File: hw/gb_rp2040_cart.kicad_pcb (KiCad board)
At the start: 2 copper layers, 51.4 x 60.5 mm, 66 parts, among them J1 GameBoy_Cartridge, J2 USB_C_Receptacle_USB2.0, Q1 SI2301CDS-T1-GE3, Q2 N-Channel, SW1 SW_SPST, U1 SN74LVC8T245PW, U10 MB85RC256VPNF-G-JNERE1, U2 SN74LVC8T245PW, U3 TXU0104, U4 SN74LVC8T245PW, U5 W25Q128JVSIQ, U6 RP2040, U7 AMS1117-3.3, U8 RV-3129-C3, U9 PCA9536D, Y1 Crystal_GND24

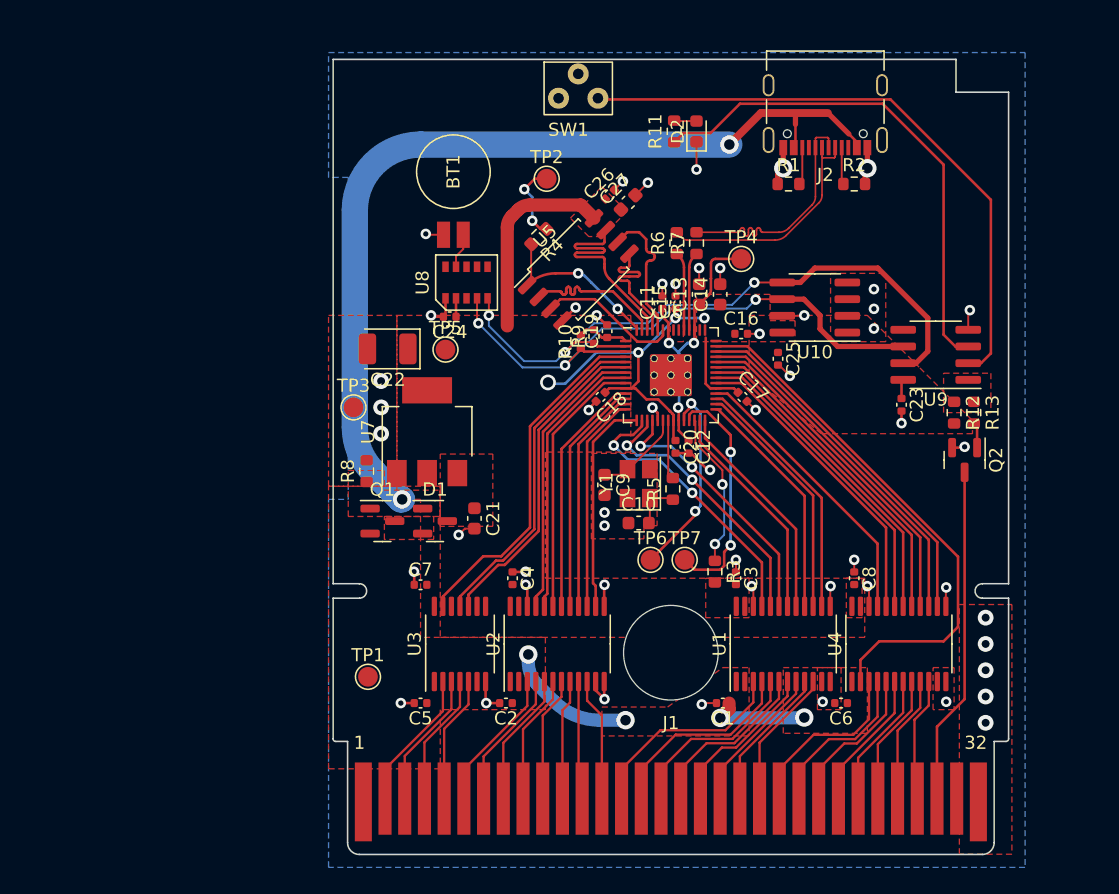
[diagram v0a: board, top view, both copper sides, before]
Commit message: hw: replace RTC
Signed-off-by: Mahyar Koshkouei <mk@deltabeard.com>
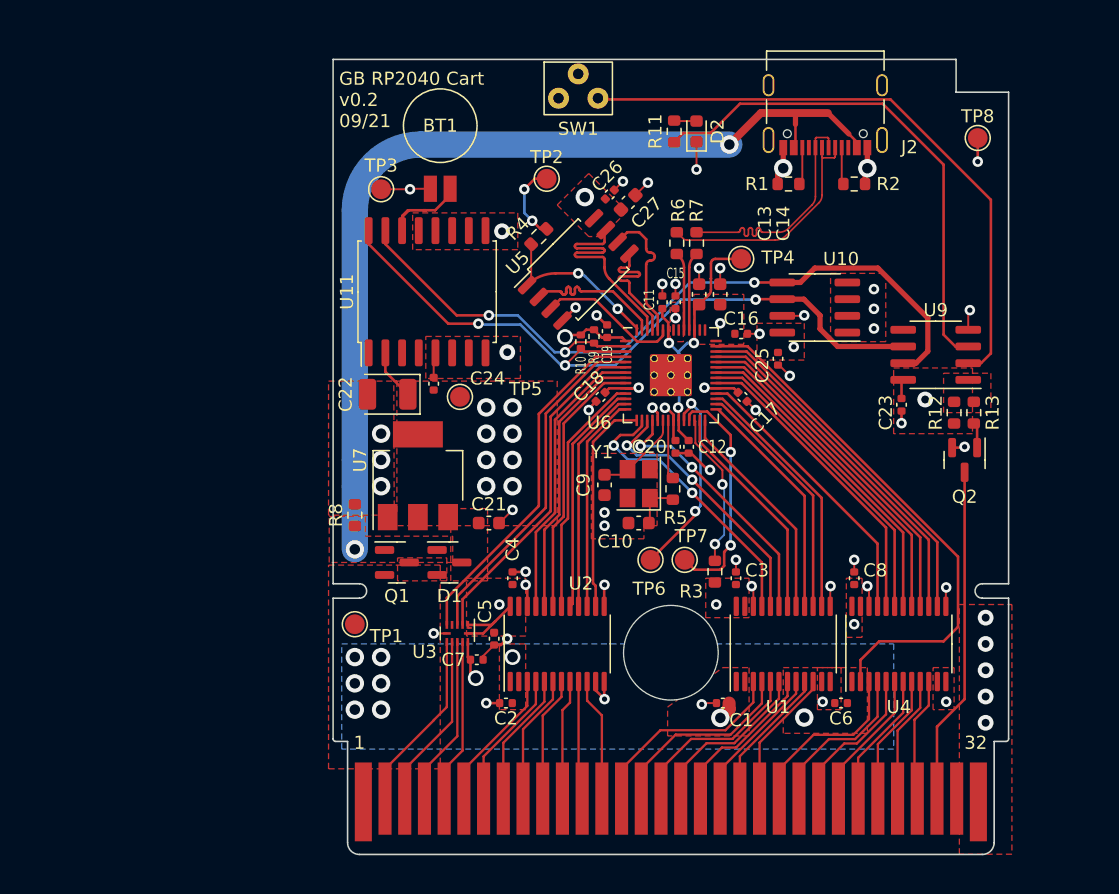
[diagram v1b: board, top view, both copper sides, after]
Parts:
- removed U8: RV-3129-C3, Project_Specific:SOIC-10_RV-3129-C3
- added TP8: GND, TestPoint:TestPoint_Pad_D1.5mm, F.Cu at (107.4, 43.5)
- added U11: DS3231M, Package_SO:SOIC-16W_7.5x10.3mm_P1.27mm, F.Cu at (65.5, 55.2)
- U3: value TXU0104 -> TXB0104RUT; footprint Package_SO:TSSOP-14_4.4x5mm_P0.65mm -> Package_DFN_QFN:Texas_R_PUQFN-N12
- moved TP3 16.7 mm to (62.0, 47.4)
- moved C5 7.44 mm to (70.6, 81.6), turned to -90 degrees
- moved C7 7.13 mm to (69.3, 83.2), turned to 180 degrees
- moved C24 5.24 mm to (66.0, 62.2), turned to 90 degrees
- moved TP1 4.12 mm to (60.0, 80.5)
- moved TP5 3.76 mm to (68.0, 63.2)
- moved BT1 3.64 mm to (66.5, 47.4)
- moved R8 3.47 mm to (60.0, 72.2)
- moved C22 3.45 mm to (62.5, 63.0)
- moved U7 3.42 mm to (64.8, 69.2)
- moved D1 3.34 mm to (67.2, 75.8)
- moved Q1 3.34 mm to (63.2, 75.8)
- moved C21 1.15 mm to (70.2, 72.8), turned to 0 degrees
- moved U3 0.82 mm to (67.8, 81.2), turned to -90 degrees
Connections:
- C5 pad 1: GB_5V -> +3V3
- C7 pad 2: +3V3 -> GB_5V
- U3 pad 1: GB_5V -> +3V3
- U3 pad 10: ~{CS}_3V3 -> ~{CS}
- U3 pad 11: ~{RD}_3V3 -> GB_5V
- U3 pad 12: ~{WR}_3V3 -> +3V3
- U3 pad 2: PHI -> ~{CS}_3V3
- U3 pad 3: ~{WR} -> ~{RD}_3V3
- U3 pad 4: ~{RD} -> ~{WR}_3V3
- U3 pad 5: ~{CS} -> PHI_3V3
- U3 pad 6: (no net) -> GND
- U3 pad 7: GND -> PHI
- U3 pad 8: +3V3 -> ~{WR}
- U3 pad 9: (no net) -> ~{RD}
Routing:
- net +3V3: track 53.9 -> 26.2 mm, vias 4 -> 20
- net GB_5V: track 17.9 -> 4.40 mm, vias 4 -> 10
- net I^{2}C_{SCL}: track 45.1 -> 54.9 mm
- net I^{2}C_{SDA}: track 50.7 -> 59.7 mm
- net Net-(BT1-Pad1): track 2.66 -> 8.99 mm
- net PHI: track 8.48 -> 13.9 mm
- net GND: track 56.2 -> 60.2 mm, vias 53 -> 55
- net ~{WR}: track 10.4 -> 13.4 mm
- net ~{RD}: track 10.0 -> 13.0 mm
- net ~{CS}: track 9.67 -> 12.5 mm
- net VBUS: track 73.7 -> 76.2 mm
- net ~{CS}_3V3: track 24.5 -> 25.9 mm
- net ~{RD}_3V3: track 25.3 -> 26.6 mm
- net PHI_3V3: track 26.7 -> 27.4 mm
- added copper zone on In2.Cu, net +3V3
- added copper zone on B.Cu, net GB_5V
- added copper zone on In1.Cu, net GND
- removed copper zone on B.Cu, net GND
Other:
- copper layers 2 -> 4
- board text added: "Flash cart compatible with DMG, MGB, CGB. Unlicensed product. Using RP2040, with 16MiB NOR, 32KiB FRAM, RTC, USB-C. Design: UK, Assembly: PRC Copyright (c) 2021 Mahyar Koshkouei; Not for resale."
- board text added: "GB RP2040 Cart v0.2 09/21"
- board text added: "JLCJLCJLCJLC"
- board text added: "Order"

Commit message: hw: complete routing
Use components available on LCSC.

Signed-off-by: Mahyar Koshkouei <mk@deltabeard.com>
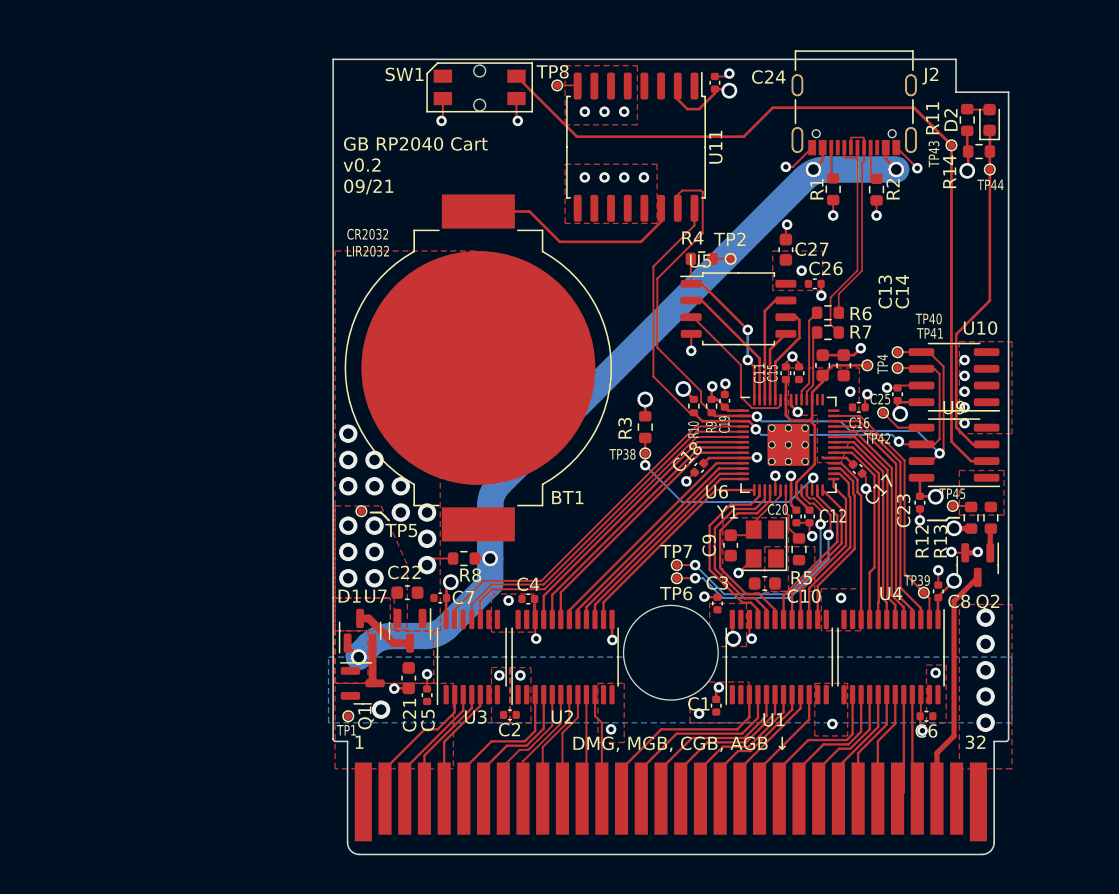
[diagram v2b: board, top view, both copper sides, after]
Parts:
- removed TP3: TestPoint, TestPoint:TestPoint_Pad_D1.5mm
- added R14: 100k, Resistor_SMD:R_0603_1608Metric, F.Cu at (107.5, 44.5)
- added TP38: TestPoint_Small, Project_Specific:TestPoint_Pad_D0.5mm, F.Cu at (82.1, 67.5)
- added TP39: TestPoint_Small, Project_Specific:TestPoint_Pad_D0.5mm, F.Cu at (103.3, 78.1)
- added TP40: TestPoint_Small, Project_Specific:TestPoint_Pad_D0.5mm, F.Cu at (101.3, 59.8)
- added TP41: TestPoint_Small, Project_Specific:TestPoint_Pad_D0.5mm, F.Cu at (101.3, 61.0)
- added TP42: TestPoint_Small, Project_Specific:TestPoint_Pad_D0.5mm, F.Cu at (100.2, 64.4)
- added TP43: TestPoint_Small, Project_Specific:TestPoint_Pad_D0.5mm, F.Cu at (105.4, 44.1)
- added TP44: TestPoint_Small, Project_Specific:TestPoint_Pad_D0.5mm, F.Cu at (108.3, 45.9)
- added TP45: TestPoint_Small, Project_Specific:TestPoint_Pad_D0.5mm, F.Cu at (105.5, 71.5)
- BT1: footprint Project_Specific:BatteryHolder_Seiko_MS621FE -> Battery:BatteryHolder_MPD_BC2003_1x2032
- C13, C14, C21, C27: value 2.2u -> 1u
- C22: value 100u -> 1u; footprint Capacitor_Tantalum_SMD:CP_EIA-3528-15_AVX-H -> Capacitor_SMD:C_0603_1608Metric
- SW1: value SW_SPST -> SW_DPST; footprint Project_Specific:Push_Button-Horizontal-TC-1109DE-C-J -> Project_Specific:K2-1114SA-A4SW-06
- TP1, TP2, TP4, TP5, TP6, TP7, TP8: footprint TestPoint:TestPoint_Pad_D1.5mm -> TestPoint:TestPoint_Pad_D1.0mm
- U3: value TXB0104RUT -> TXU0104; footprint Package_DFN_QFN:Texas_R_PUQFN-N12 -> Package_SO:TSSOP-14_4.4x5mm_P0.65mm
- U7: value AMS1117-3.3 -> XC6206P332MR; footprint Package_TO_SOT_SMD:SOT-223-3_TabPin2 -> Package_TO_SOT_SMD:SOT-23
- moved TP8 32.2 mm to (75.4, 39.5)
- moved C24 31.3 mm to (87.4, 39.3)
- moved D2 22.3 mm to (108.3, 42.1)
- moved R11 22.3 mm to (106.6, 42.1)
- moved U11 19.3 mm to (81.4, 44.2), turned to -90 degrees
- moved C26 17.0 mm to (95.0, 54.6), turned to 0 degrees
- moved TP2 15.3 mm to (88.6, 52.7)
- moved C22 15.2 mm to (64.0, 78.1), turned to 0 degrees
- moved BT1 13.9 mm to (69.4, 61.0)
- moved C21 13.3 mm to (64.1, 84.6), turned to -90 degrees
- moved R6 12.7 mm to (96.0, 56.8), turned to 0 degrees
- moved U5 12.6 mm to (89.2, 56.5), turned to 0 degrees
- moved TP4 12.6 mm to (99.0, 60.8)
- moved C27 12.5 mm to (92.8, 52.0), turned to 90 degrees
- moved R4 12.5 mm to (86.4, 52.7), turned to 180 degrees
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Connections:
- net GB_RESET renamed /Peripherals/GB_RESET
- C5 pad 1: +3V3 -> GB_5V
- C7 pad 2: GB_5V -> +3V3
- D2 pad 1: GND -> /Peripherals/STAT_LED
- R11 pad 1: Net-(R11-Pad1) -> +3V3
- SW1 pad 1: Net-(SW1-Pad1) -> /Peripherals/SWITCH
- SW1 pad 3: (no net) -> /Peripherals/SWITCH
- U3 pad 1: +3V3 -> GB_5V
- U3 pad 10: ~{CS} -> ~{CS}_3V3
- U3 pad 11: GB_5V -> ~{RD}_3V3
- U3 pad 12: +3V3 -> ~{WR}_3V3
- U3 pad 2: ~{CS}_3V3 -> PHI
- U3 pad 3: ~{RD}_3V3 -> ~{WR}
- U3 pad 4: ~{WR}_3V3 -> ~{RD}
- U3 pad 5: PHI_3V3 -> ~{CS}
- U3 pad 6: GND -> (no net)
- U3 pad 7: PHI -> GND
- U3 pad 8: ~{WR} -> +3V3
- U3 pad 9: ~{RD} -> (no net)
- U4 pad 1: GB_5V -> +3V3
- U4 pad 10: /D7 -> 3V3_D0
- U4 pad 14: 3V3_D7 -> /D0
- U4 pad 15: 3V3_D6 -> /D1
- U4 pad 16: 3V3_D5 -> /D2
- U4 pad 17: 3V3_D4 -> /D3
- U4 pad 18: 3V3_D3 -> /D4
- U4 pad 19: 3V3_D2 -> /D5
- U4 pad 20: 3V3_D1 -> /D6
- U4 pad 21: 3V3_D0 -> /D7
- U4 pad 23: +3V3 -> GB_5V
- U4 pad 24: +3V3 -> GB_5V
- U4 pad 3: /D0 -> 3V3_D7
- U4 pad 4: /D1 -> 3V3_D6
- U4 pad 5: /D2 -> 3V3_D5
- U4 pad 6: /D3 -> 3V3_D4
- U4 pad 7: /D4 -> 3V3_D3
- U4 pad 8: /D5 -> 3V3_D2
- U4 pad 9: /D6 -> 3V3_D1
- U9 pad 2: Net-(SW1-Pad1) -> /Peripherals/SWITCH
- U9 pad 3: Net-(R11-Pad1) -> /Peripherals/STAT_LED
- U9 pad 5: unconnected-(U9-Pad5) -> Net-(TP42-Pad1)
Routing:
- net /Peripherals/SWITCH: track 0.00 -> 100.3 mm
- net Net-(SW1-Pad1): track 46.7 -> 0.00 mm
- net Net-(R11-Pad1): track 38.8 -> 0.00 mm
- net /Peripherals/STAT_LED: track 0.00 -> 37.9 mm
- net DATA_DIR: track 40.5 -> 19.7 mm
- net +3V3: track 26.2 -> 40.4 mm, vias 20 -> 23
- net VBUS: track 76.2 -> 66.2 mm, vias 2 -> 4
- net 3V3_D3: track 24.9 -> 16.1 mm
- net 3V3_D5: track 26.3 -> 17.5 mm
- net 3V3_D4: track 25.6 -> 16.8 mm
- net 3V3_D2: track 24.2 -> 15.4 mm
- net 3V3_D6: track 27.0 -> 18.3 mm
- net 3V3_D7: track 27.7 -> 19.0 mm
- net 3V3_D0: track 21.8 -> 13.1 mm
- net 3V3_D1: track 23.5 -> 14.9 mm
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- added copper zone on F.Cu, net Net-(C10-Pad2)
- removed copper zone on F.Cu, net Net-(D1-Pad2)
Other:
- outline, holes or cut-outs redrawn
- board text added: "CR2032 LIR2032"
- board text added: "DMG, MGB, CGB, AGB ↓"
- board text added: "Flash cart compatible with DMG, MGB, CGB, AGB. Unlicensed product. Uses RP2040 with 16MiB NOR, 32KiB FRAM, RTC, USB-C. Design: United Kingdom, Assembly: P.R. China Copyright © 2021 Mahyar Koshkouei; Not for resale."
- board text added: "Order #"
- board text added: "git.io/JEM5x"
- board text removed: "Flash cart compatible with DMG, MGB, CGB. Unlicensed product. Using RP2040, with 16MiB NOR, 32KiB FRAM, RTC, USB-C. Design: UK, Assembly: PRC Copyright (c) 2021 Mahyar Koshkouei; Not for resale."
- board text removed: "Order"

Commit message: hw: fix USB
Additionally reduced the size of the battery holder.

Signed-off-by: Mahyar Koshkouei <mk@deltabeard.com>
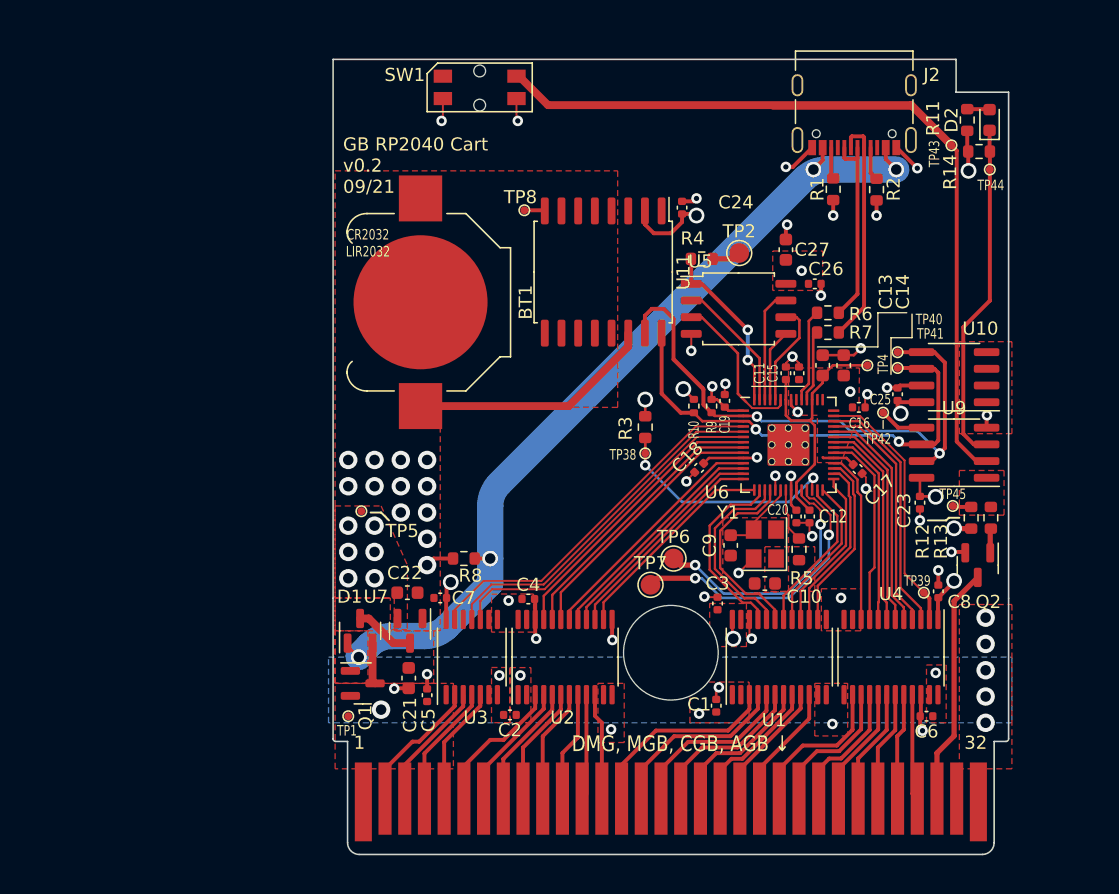
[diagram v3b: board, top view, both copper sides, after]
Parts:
- BT1: footprint Battery:BatteryHolder_MPD_BC2003_1x2032 -> Battery:BatteryHolder_Keystone_3000_1x12mm
- TP2, TP6, TP7: footprint TestPoint:TestPoint_Pad_D1.0mm -> TestPoint:TestPoint_Pad_D1.5mm
- moved C24 9.82 mm to (84.9, 48.8)
- moved TP8 9.82 mm to (72.9, 49.0)
- moved U11 9.82 mm to (78.9, 53.7)
- moved BT1 6.66 mm to (65.0, 56.0)
- moved TP7 2.06 mm to (82.5, 77.5)
- moved TP2 0.79 mm to (89.2, 52.2)
- moved TP6 0.56 mm to (84.2, 75.5)
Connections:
- J2 pad A6: USB_DN -> USB_DP
- J2 pad A7: USB_DP -> USB_DN
- J2 pad B6: USB_DN -> USB_DP
- J2 pad B7: USB_DP -> USB_DN
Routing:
- net I^{2}C_{SCL}: track 46.5 -> 35.8 mm
- net /Peripherals/SWITCH: track 100.3 -> 90.5 mm
- net /Peripherals/STAT_LED: track 37.9 -> 47.3 mm
- net Net-(R7-Pad1): track 5.02 -> 9.16 mm
- net /A3: track 6.54 -> 9.10 mm
- net /D3: track 6.74 -> 9.16 mm
- net /D2: track 7.77 -> 10.0 mm
- net /A14: track 7.57 -> 9.82 mm
- net /A15: track 7.22 -> 9.47 mm
- net Net-(BT1-Pad1): track 16.5 -> 18.7 mm
- net /A13: track 8.48 -> 10.7 mm
- net /RP2040/SWDIO: track 19.7 -> 21.9 mm
- net /A12: track 9.44 -> 11.6 mm
- net /D1: track 8.72 -> 10.9 mm
- net /A11: track 10.4 -> 12.5 mm
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
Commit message: hw: add BOOTSEL button and routing changes
Signed-off-by: Mahyar Koshkouei <mk@deltabeard.com>
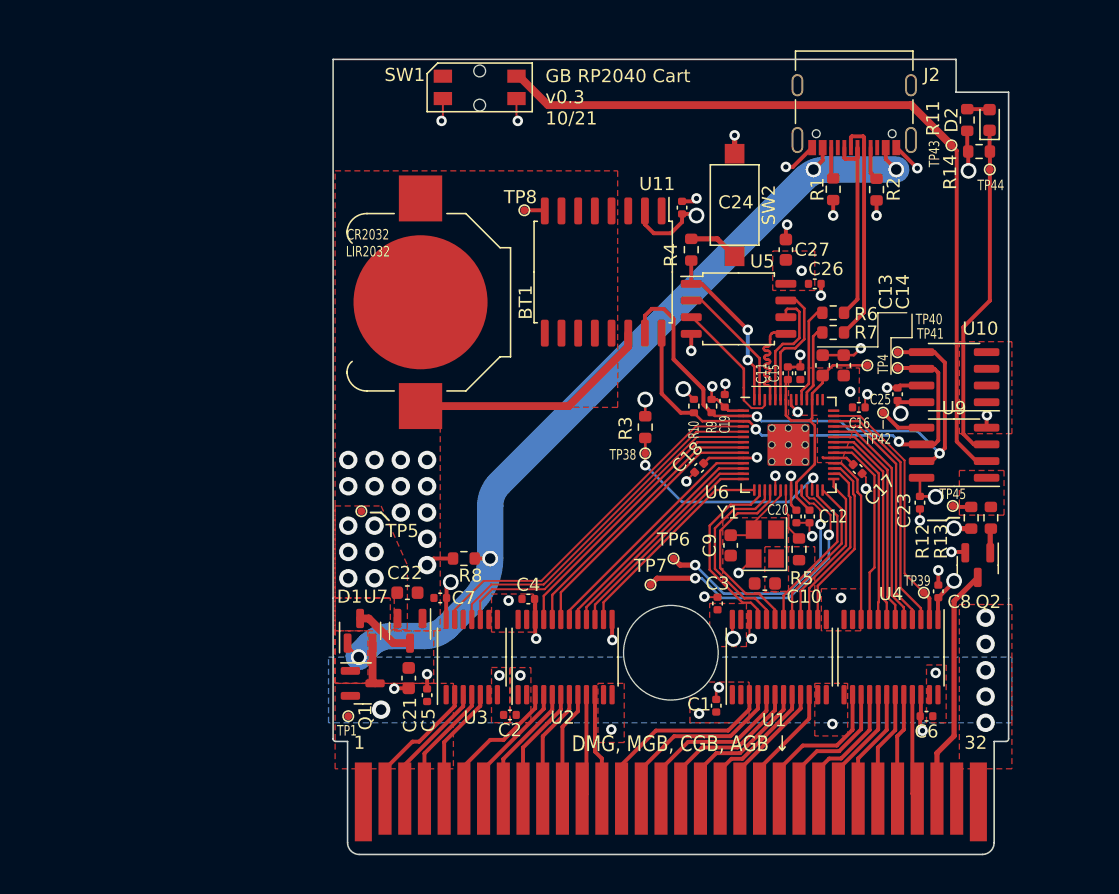
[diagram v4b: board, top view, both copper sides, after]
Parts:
- removed TP2: TestPoint, TestPoint:TestPoint_Pad_D1.5mm
- added SW2: SW_Push, Button_Switch_SMD:SW_SPST_CK_RS282G05A3, F.Cu at (88.9, 48.6)
- TP6, TP7: footprint TestPoint:TestPoint_Pad_D1.5mm -> TestPoint:TestPoint_Pad_D1.0mm
- moved R4 1.06 mm to (85.6, 52.0), turned to -90 degrees
- moved R6 0.40 mm to (96.4, 56.8)
- moved R7 0.40 mm to (96.4, 58.3)
- moved C11 0.15 mm to (93.0, 61.4)
- moved C15 0.10 mm to (93.9, 61.4)
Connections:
- U5 pad 3: /RP2040/QSPI_SD3 -> /RP2040/QSPI_SD2
- U5 pad 7: /RP2040/QSPI_SD2 -> /RP2040/QSPI_SD3
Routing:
- net /Peripherals/SWITCH: track 90.5 -> 75.8 mm
- net /RP2040/QSPI_SD0: track 5.51 -> 9.08 mm
- net /RP2040/QSPI_SD3: track 12.0 -> 9.82 mm
- net /RP2040/QSPI_SD2: track 8.68 -> 10.4 mm
- net /RP2040/QSPI_SCLK: track 7.93 -> 9.62 mm
- net /RP2040/USB_BOOT: track 2.21 -> 3.85 mm
- net GND: track 52.6 -> 54.0 mm, vias 53 -> 54
- net /RP2040/SWCLK: track 20.9 -> 19.5 mm
- net USB_DP: track 15.0 -> 15.6 mm
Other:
- board text added: "GB RP2040 Cart v0.3 10/21"
- board text removed: "GB RP2040 Cart v0.2 09/21"
